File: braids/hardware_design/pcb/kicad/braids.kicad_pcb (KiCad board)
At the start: 2 copper layers, 78.7 x 106.7 mm, 120 parts, among them IC1 74HC595D, IC10 TL072, IC2 74HC595D, IC3 LM4040B25, IC4 MCP3204, IC5 DAC8551, IC6 LM1117-3.3, IC7 MCP6004, IC8 LM4040B10, IC9 TL074D, J1 PJ301_THONKICONN6, J2 PJ301_THONKICONN6, J3 PJ301_THONKICONN6, J4 PJ301_THONKICONN6, J5 PJ301_THONKICONN6, J6 PJ301_THONKICONN6, Q1 MMBT3904, Q2 MMBT3904, Q3 MMBT3904, Q4 MMBT3904, Q5 8MHz, Q6 MMBT3904, SW1 EC12E_SW

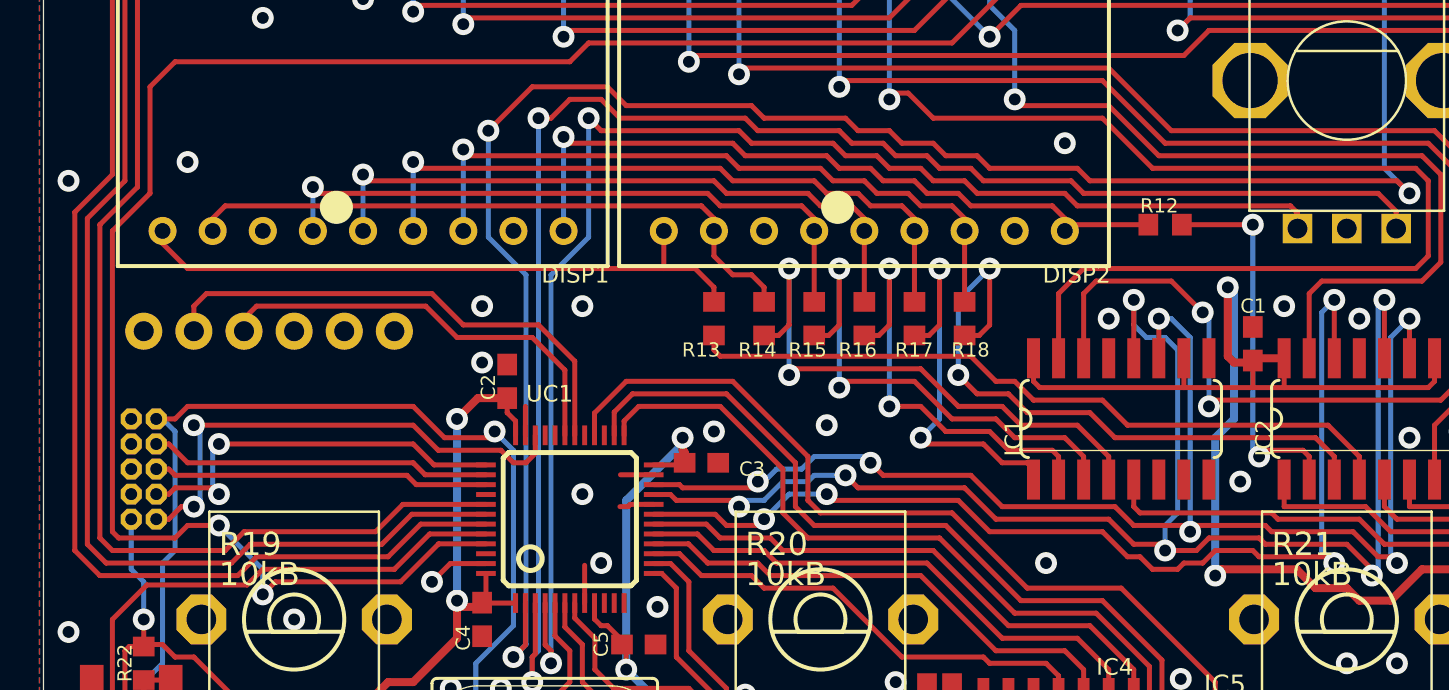
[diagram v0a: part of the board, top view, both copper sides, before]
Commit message: add surfact mount serial flashing header
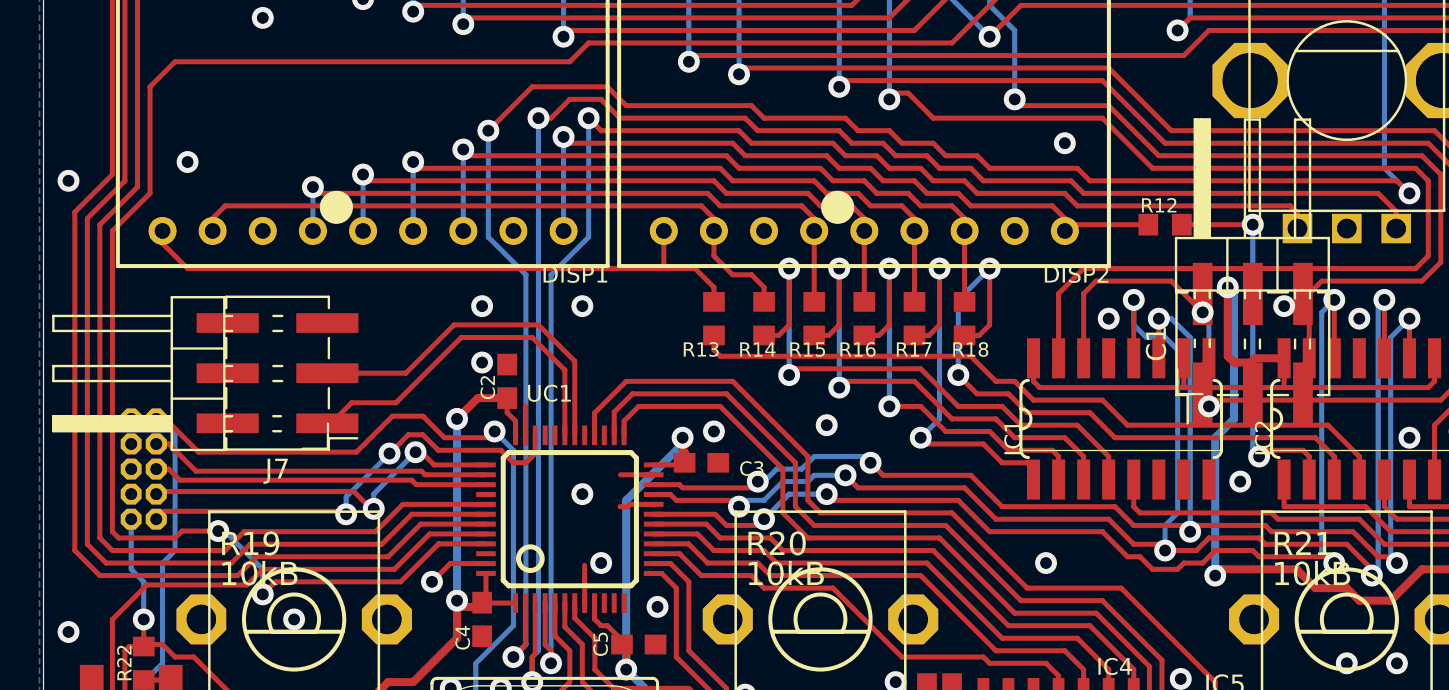
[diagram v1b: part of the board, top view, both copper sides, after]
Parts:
- removed JP3: , braids:1X06
- added J7: Conn_02x03_Odd_Even, Connector_PinHeader_2.54mm:PinHeader_2x03_P2.54mm_Horizontal_SMD, F.Cu at (121.0, 83.0)
- C1: footprint braids:C0603 -> Connector_PinHeader_2.54mm:PinHeader_2x03_P2.54mm_Horizontal_SMD
- IC1, IC2: value 74HC595D -> 74595D
- SW2, SW3: value (none) -> EVQQ2
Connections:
- net ADC_MISO renamed /braids_2/ADC_MISO
- net ADC_MOSI renamed /braids_2/ADC_MOSI
- net ADC_SCK renamed /braids_2/ADC_SCK
- net ADC_SS renamed /braids_2/ADC_SS
- net BOOT_FLASH renamed /braids_2/BOOT_FLASH
- net DAC_MOSI renamed /braids_2/DAC_MOSI
- net DAC_SCK renamed /braids_2/DAC_SCK
- net DAC_SS renamed /braids_2/DAC_SS
- net DISP_CHAR0 renamed /braids_2/DISP_CHAR0
- net DISP_CHAR1 renamed /braids_2/DISP_CHAR1
- net DISP_CHAR2 renamed /braids_2/DISP_CHAR2
- net DISP_CHAR3 renamed /braids_2/DISP_CHAR3
- net DISP_EN renamed /braids_2/DISP_EN
- net DISP_SCK renamed /braids_2/DISP_SCK
- net DISP_SER renamed /braids_2/DISP_SER
- net ENC_A renamed /braids_2/ENC_A
- net ENC_B renamed /braids_2/ENC_B
- net ENC_CLICK renamed /braids_2/ENC_CLICK
- net FINE_TUNE renamed /braids_2/FINE_TUNE
- net JTCK renamed /braids_2/JTCK
- net JTDI renamed /braids_2/JTDI
- net JTDO renamed /braids_2/JTDO
- net JTMS renamed /braids_2/JTMS
- net RESET renamed /braids_2/RESET
- DISP1 pad 8: (no net) -> unconnected-(DISP1-Pad8)
- DISP2 pad 8: (no net) -> unconnected-(DISP2-Pad8)
- IC1 pad 6: (no net) -> unconnected-(IC1-Pad6)
- IC1 pad 7: (no net) -> unconnected-(IC1-Pad7)
- IC1 pad 9: (no net) -> unconnected-(IC1-Pad9)
- J1 pad P2: (no net) -> unconnected-(J1-PadP2)
- J2 pad P2: (no net) -> unconnected-(J2-PadP2)
- J3 pad P2: (no net) -> unconnected-(J3-PadP2)
- J4 pad P2: (no net) -> unconnected-(J4-PadP2)
- J5 pad P2: (no net) -> unconnected-(J5-PadP2)
- J6 pad P2: (no net) -> unconnected-(J6-PadP2)
- JP2 pad 7: (no net) -> unconnected-(JP2-Pad7)
- UC1 pad 10: (no net) -> unconnected-(UC1-Pad10)
- UC1 pad 11: (no net) -> unconnected-(UC1-Pad11)
- UC1 pad 12: (no net) -> unconnected-(UC1-Pad12)
- UC1 pad 27: (no net) -> unconnected-(UC1-Pad27)
- UC1 pad 29: (no net) -> unconnected-(UC1-Pad29)
- UC1 pad 30: TX -> /braids_2/TX
- UC1 pad 31: RX -> /braids_2/RX
- UC1 pad 32: (no net) -> unconnected-(UC1-Pad32)
- UC1 pad 33: (no net) -> unconnected-(UC1-Pad33)
- UC1 pad 40: (no net) -> unconnected-(UC1-Pad40)
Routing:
- net +3V3: track 327.3 -> 519.0 mm, vias 13 -> 20
- net Net-(IC1-Pad15): track 71.2 -> 0.00 mm, vias 2 -> 0
- net Net-(IC2-Pad15): track 54.1 -> 0.00 mm, vias 2 -> 0
- net Net-(IC2-Pad4): track 36.8 -> 0.00 mm
- net Net-(IC1-Pad14): track 29.5 -> 0.00 mm, vias 2 -> 0
- net TX: track 26.0 -> 0.00 mm
- net RX: track 21.8 -> 0.00 mm
- net /braids_2/TX: track 0.00 -> 18.1 mm
- net /braids_2/RX: track 0.00 -> 17.8 mm
- net /braids_2/JTMS: track 25.8 -> 23.3 mm
- net /braids_2/JTCK: track 20.4 -> 19.0 mm
- net /braids_2/RESET: track 95.7 -> 96.7 mm
- net GND: vias 109 -> 108

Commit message: move new header
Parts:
- C1: footprint Connector_PinHeader_2.54mm:PinHeader_2x03_P2.54mm_Horizontal_SMD -> braids:C0603
- moved J7 59.5 mm to (121.0, 142.5)
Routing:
- net +3V3: track 519.0 -> 327.3 mm, vias 20 -> 13
- net Net-(IC1-Pad15): track 0.00 -> 71.2 mm, vias 0 -> 2
- net /braids_2/RX: track 17.8 -> 81.7 mm, vias 0 -> 2
- net /braids_2/TX: track 18.1 -> 77.8 mm, vias 0 -> 2
- net Net-(IC2-Pad15): track 0.00 -> 54.1 mm, vias 0 -> 2
- net Net-(IC2-Pad4): track 0.00 -> 36.8 mm
- net Net-(IC1-Pad14): track 0.00 -> 29.5 mm, vias 0 -> 2
- net VEE: track 117.8 -> 119.0 mm
- net GND: vias 108 -> 110

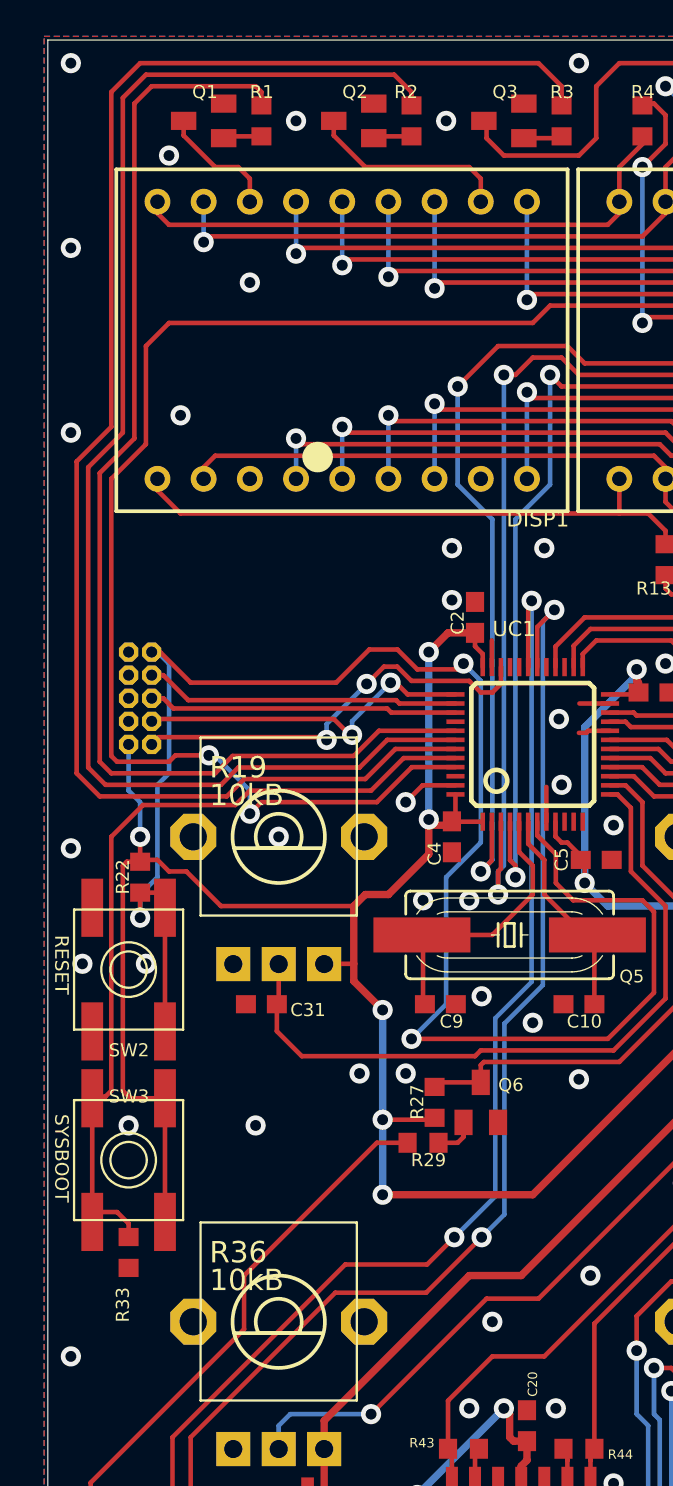
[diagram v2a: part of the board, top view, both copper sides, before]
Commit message: re-routing some traces around the jtag connector
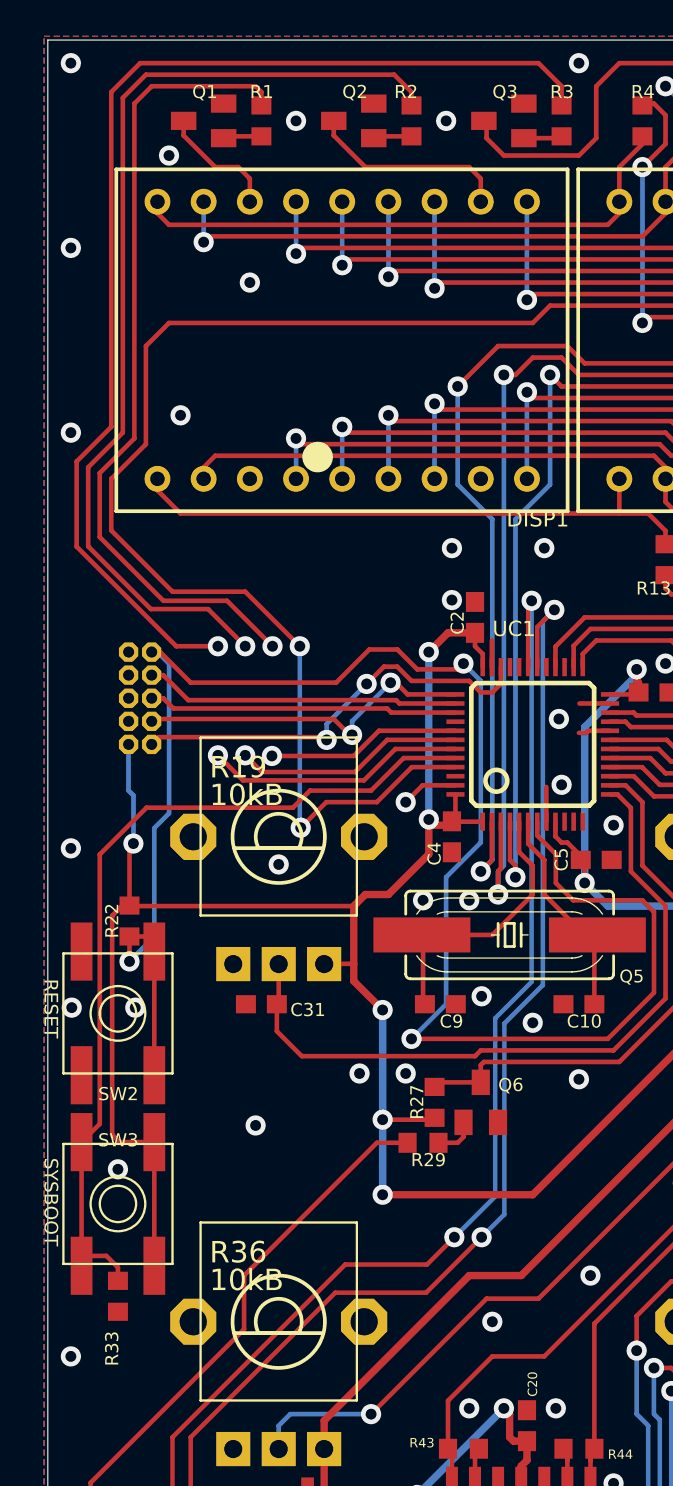
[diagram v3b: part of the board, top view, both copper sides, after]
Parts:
- moved R22 2.48 mm to (113.6, 100.1)
- moved R33 2.48 mm to (113.0, 120.7)
- moved SW2 2.48 mm to (113.0, 105.2)
- moved SW3 2.48 mm to (113.0, 115.7)
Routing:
- net /braids_2/DISP_CHAR0: track 87.7 -> 77.2 mm, vias 0 -> 2
- net /braids_2/DISP_CHAR2: track 66.0 -> 55.5 mm, vias 0 -> 2
- net /braids_2/DISP_CHAR3: track 76.8 -> 66.6 mm, vias 0 -> 2
- net /braids_2/RESET: track 96.7 -> 99.3 mm
- net /braids_2/BOOT_FLASH: track 45.7 -> 47.8 mm
- net /braids_2/DISP_CHAR1: track 105.9 -> 104.0 mm
- net +3V3: track 327.3 -> 329.0 mm

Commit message: fix DRC
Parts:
- JP2: footprint braids:2X5-1.27 -> braids:AVR_ICSP
- moved JP2 2.89 mm to (112.0, 87.0)
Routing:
- net /braids_2/RESET: track 99.3 -> 106.2 mm
- net GND: track 10.1 -> 16.2 mm
- net /braids_2/DISP_CHAR0: track 77.2 -> 80.4 mm
- net /braids_2/DISP_CHAR1: track 104.0 -> 101.0 mm
- net /braids_2/DISP_CHAR3: track 66.6 -> 69.4 mm
- net /braids_2/DISP_CHAR2: track 55.5 -> 58.3 mm
- net /braids_2/JTDI: track 17.4 -> 19.8 mm
- net /braids_2/JTMS: track 23.3 -> 25.6 mm
- net /braids_2/JTDO: track 17.0 -> 19.0 mm
- net /braids_2/JTCK: track 19.0 -> 20.8 mm
- net +3V3: track 329.0 -> 328.3 mm
- net /braids_2/BOOT_FLASH: track 47.8 -> 47.2 mm

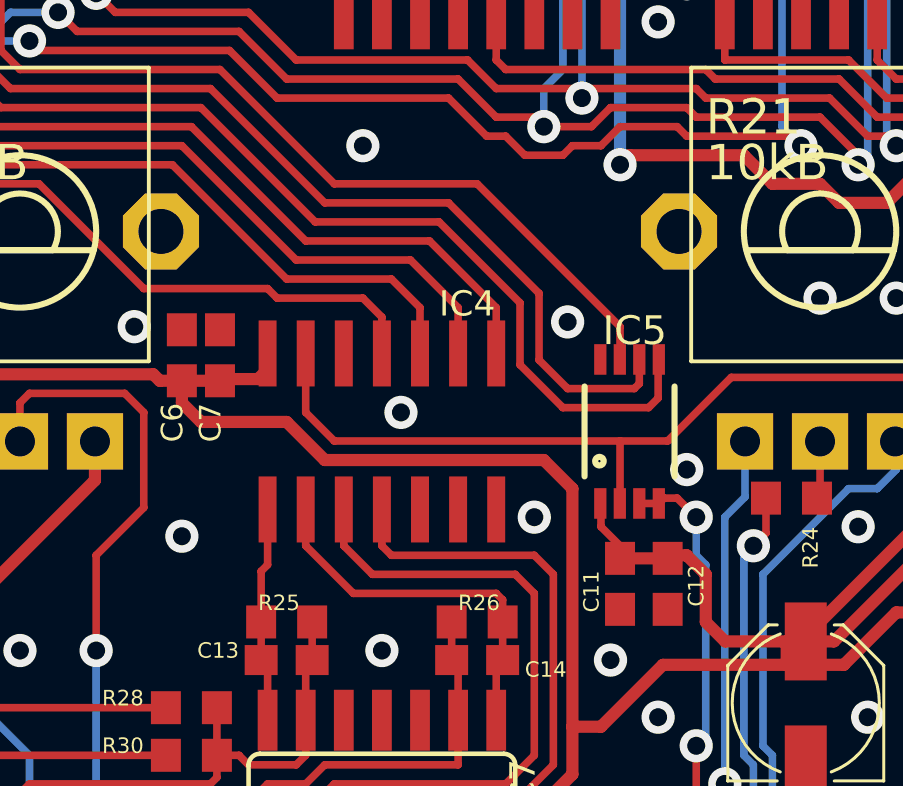
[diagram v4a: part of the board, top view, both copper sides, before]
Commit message: changed mcp3204 to mcp3208
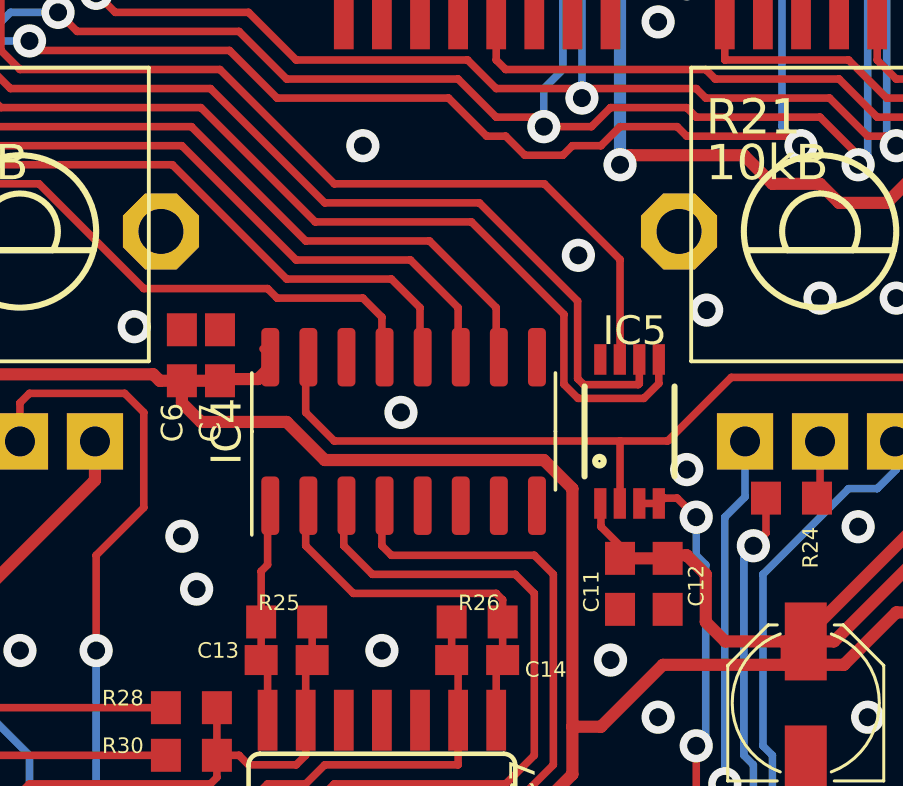
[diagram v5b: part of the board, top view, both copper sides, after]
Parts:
- IC4: value MCP3204 -> MCP3208; footprint braids:SO14 -> Package_SO:SOIC-16_3.9x9.9mm_P1.27mm
- moved IC4 0.72 mm to (161.3, 102.1), turned to 90 degrees
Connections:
- IC4 pad 10: /braids_2/ADC_MISO -> /braids_2/ADC_SS
- IC4 pad 11: /braids_2/ADC_SCK -> /braids_2/ADC_MOSI
- IC4 pad 12: GND -> /braids_2/ADC_MISO
- IC4 pad 13: AREF -> /braids_2/ADC_SCK
- IC4 pad 14: +3V3 -> GND
- IC4 pad 5: (no net) -> unconnected-(IC4-Pad5)
- IC4 pad 6: (no net) -> unconnected-(IC4-Pad6)
- IC4 pad 7: GND -> unconnected-(IC4-Pad7)
- IC4 pad 8: /braids_2/ADC_SS -> unconnected-(IC4-Pad8)
- IC4 pad 9: /braids_2/ADC_MOSI -> GND
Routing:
- net /braids_2/DAC_MOSI: track 42.0 -> 43.3 mm
- net GND: vias 110 -> 111
